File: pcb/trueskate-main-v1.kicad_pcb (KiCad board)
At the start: 2 copper layers, 160 x 120 mm, 153 parts, among them J1 Teensy 4.1 FEMALE 1x24, J11 Mini v1.0 FEMALE sockets, J12 Mini v1.0 FEMALE sockets, J13 Mini v1.0 FEMALE sockets, J14 Mini v1.0 FEMALE sockets, J15 Mini v1.0 FEMALE sockets, J16 Mini v1.0 FEMALE sockets, J2 Teensy 4.1 FEMALE 1x24, J21 MOTOR PHASES male 1x3, J22 MOTOR PHASES male 1x3, J23 MOTOR PHASES male 1x3, J24 MOTOR PHASES male 1x3, J25 MOTOR PHASES male 1x3, J26 MOTOR PHASES male 1x3, J3 VUSB from isolated Teensy pad, J31 ENCODER JST-SH 6p, J32 ENCODER JST-SH 6p, J33 ENCODER JST-SH 6p, J34 ENCODER JST-SH 6p, J35 ENCODER JST-SH 6p, J36 ENCODER JST-SH 6p, J4 NC KILL SWITCH, J41 MINI POWER: +12V / GND, J42 MINI POWER: +12V / GND, J43 MINI POWER: +12V / GND, J44 MINI POWER: +12V / GND, J45 MINI POWER: +12V / GND, J46 MINI POWER: +12V / GND, J5 12V INPUT 5.08mm >=10A, J6 WRIST: GND / 12V / DATA, J7 FUTURE I2C / 3V3 ONLY, J8 FINGERTIP 1 GND, J9 FINGERTIP 2 GND, Q1 FQP47P06 reverse-polarity, Q2 FQP47P06 servo power switch, Q3 MMBT3904 transmit enable, Q4 MMBT3904 kill power control, U1 SN74LVC08APWR, U2 SN74LVC08APWR, U3 SN74LVC1G17DBVR, U4 AP63205WU-7 fixed 5V, U5 SN74AHCT1G125DBVR TX, U6 SN74LVC1G125DBVR RX

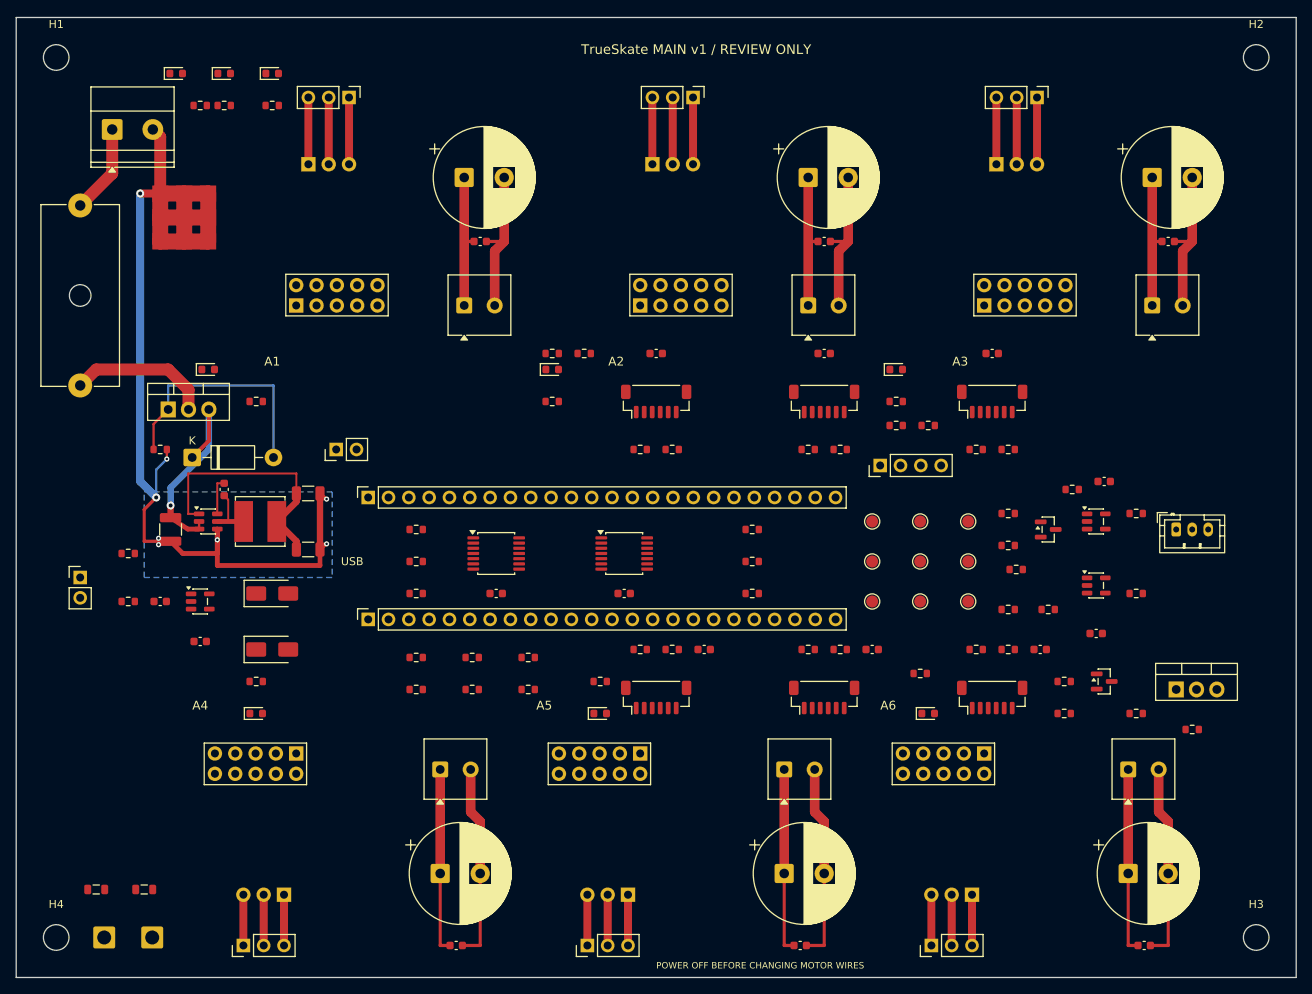
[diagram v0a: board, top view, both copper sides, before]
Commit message: feat: finish through-hole six-axis carrier review design
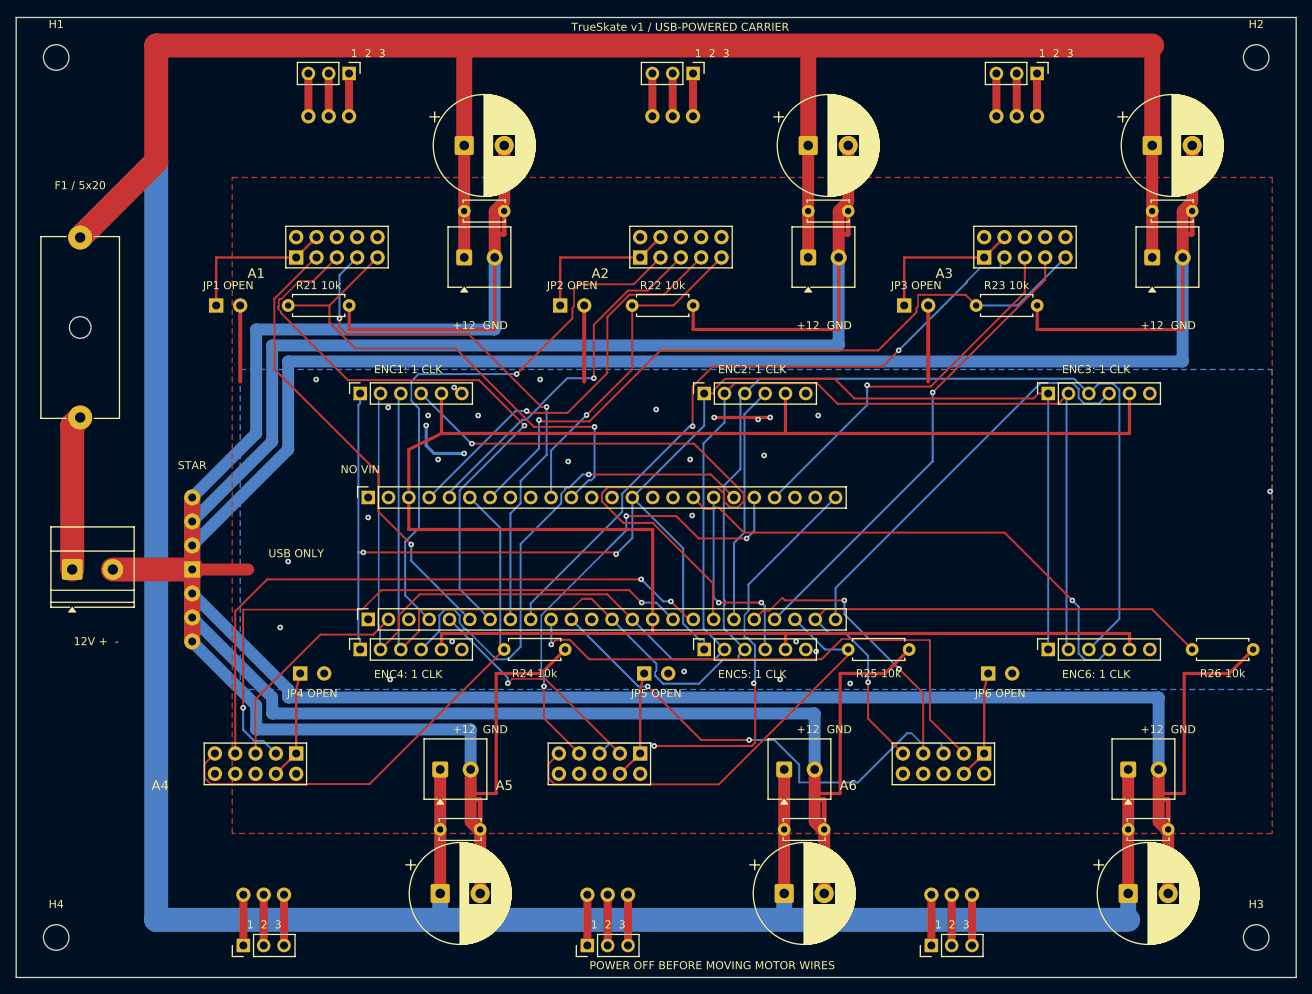
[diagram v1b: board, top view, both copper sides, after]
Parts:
- removed C1: 1nF 50V, Capacitor_SMD:C_0603_1608Metric
- removed C2, C3, C31, C32, C33, C34, C35, C36, C37, C38, C4: 100nF 50V, Capacitor_SMD:C_0603_1608Metric
- removed C5: 10uF 50V X7R, Capacitor_SMD:C_1210_3225Metric
- removed C6: 100nF bootstrap, Capacitor_SMD:C_0603_1608Metric
- removed C7, C8: 22uF 25V X5R, Capacitor_SMD:C_1206_3216Metric
- removed D1, D2: SS14 Schottky, Diode_SMD:D_SMA
- removed D11, D12, D13, D14, D15, D16, D17, D18, D19: KT-0603R red indicator, LED_SMD:LED_0603_1608Metric
- removed D3: 1N4742A 12V gate clamp, Diode_THT:D_DO-41_SOD81_P10.16mm_Horizontal
- removed FB1, FB2: BLM21PG221SN1D ferrite, Inductor_SMD:L_0805_2012Metric
- removed J3: VUSB from isolated Teensy pad, Connector_PinHeader_2.54mm:PinHeader_1x02_P2.54mm_Vertical
- removed J4: NC KILL SWITCH, Connector_PinHeader_2.54mm:PinHeader_1x02_P2.54mm_Vertical
- removed J6: WRIST: GND / 12V / DATA, Connector_JST:JST_PH_B3B-PH-K_1x03_P2.00mm_Vertical
- removed J7: FUTURE I2C / 3V3 ONLY, Connector_PinHeader_2.54mm:PinHeader_1x04_P2.54mm_Vertical
- removed J8: FINGERTIP 1 GND, Connector_Wire:SolderWire-1sqmm_1x01_D1.4mm_OD2.7mm
- removed J9: FINGERTIP 2 GND, Connector_Wire:SolderWire-1sqmm_1x01_D1.4mm_OD2.7mm
- removed L1: SRN6045TA-4R7M 4.7uH, Inductor_SMD:L_Bourns_SRN6045TA
- removed Q1: FQP47P06 reverse-polarity, Package_TO_SOT_THT:TO-220-3_Vertical
- removed Q2: FQP47P06 servo power switch, Package_TO_SOT_THT:TO-220-3_Vertical
- removed Q3: MMBT3904 transmit enable, Package_TO_SOT_SMD:SOT-23
- removed Q4: MMBT3904 kill power control, Package_TO_SOT_SMD:SOT-23
- removed R1: 1k, Resistor_SMD:R_0603_1608Metric
- removed R11, R12, R13, R14, R15, R16: 10k EN boot pulldown, Resistor_SMD:R_0603_1608Metric
- removed R2, R4, R52, R6: 10k, Resistor_SMD:R_0603_1608Metric
- removed R3, R5, R53: 100k, Resistor_SMD:R_0603_1608Metric
- removed R31, R32, R33, R34, R35, R36: 10k CS idle pullup, Resistor_SMD:R_0603_1608Metric
- removed R41, R42, R43, R44, R45, R46: 33R CS source damping, Resistor_SMD:R_0603_1608Metric
- removed R51: 100k gate off, Resistor_SMD:R_0603_1608Metric
- removed R54, R55: 4.7k, Resistor_SMD:R_0603_1608Metric
- removed R56, R57: 33R source damping, Resistor_SMD:R_0603_1608Metric
- removed R58: 10k TX boot pulldown, Resistor_SMD:R_0603_1608Metric
- removed R59: 100k bus off-state bias, Resistor_SMD:R_0603_1608Metric
- removed R60: 10k UART idle pullup, Resistor_SMD:R_0603_1608Metric
- removed R61, R62, R63, R64, R65, R66, R67, R68, R69: 4.7k LED limit, Resistor_SMD:R_0603_1608Metric
- removed R7: 100R bus series, Resistor_SMD:R_0603_1608Metric
- removed R8: 2.2k bus idle pullup / DNP, Resistor_SMD:R_0603_1608Metric
- removed R9: 10k gate sink, Resistor_SMD:R_0603_1608Metric
- removed TP1: GND, TestPoint:TestPoint_Pad_D1.5mm
- removed TP2: 12V_PROTECTED, TestPoint:TestPoint_Pad_D1.5mm
- removed TP3: BUCK_5V, TestPoint:TestPoint_Pad_D1.5mm
- removed TP4: VIN_OR, TestPoint:TestPoint_Pad_D1.5mm
- removed TP5: 3V3, TestPoint:TestPoint_Pad_D1.5mm
- removed TP6: SPI_SCK_CABLE, TestPoint:TestPoint_Pad_D1.5mm
- removed TP7: SPI_MOSI_CABLE, TestPoint:TestPoint_Pad_D1.5mm
- removed TP8: SPI_MISO, TestPoint:TestPoint_Pad_D1.5mm
- removed TP9: KILL_OK, TestPoint:TestPoint_Pad_D1.5mm
- removed U1, U2: SN74LVC08APWR, Package_SO:TSSOP-14_4.4x5mm_P0.65mm
- removed U3: SN74LVC1G17DBVR, Package_TO_SOT_SMD:SOT-23-5
- removed U4: AP63205WU-7 fixed 5V, Package_TO_SOT_SMD:TSOT-23-6
- removed U5: SN74AHCT1G125DBVR TX, Package_TO_SOT_SMD:SOT-23-5
- removed U6: SN74LVC1G125DBVR RX, Package_TO_SOT_SMD:SOT-23-5
- added JP1: CONTROL GND / OPEN, TrueSkate:GroundBridge_THT, F.Cu at (25.0, 36.0)
- added JP2: CONTROL GND / OPEN, TrueSkate:GroundBridge_THT, F.Cu at (68.0, 36.0)
- added JP3: CONTROL GND / OPEN, TrueSkate:GroundBridge_THT, F.Cu at (111.0, 36.0)
- added JP4: CONTROL GND / OPEN, TrueSkate:GroundBridge_THT, F.Cu at (35.5, 82.0)
- added JP5: CONTROL GND / OPEN, TrueSkate:GroundBridge_THT, F.Cu at (78.5, 82.0)
- added JP6: CONTROL GND / OPEN, TrueSkate:GroundBridge_THT, F.Cu at (121.5, 82.0)
- C11, C12, C13, C14, C15, C16: value EEUFR1V102B 1000uF 35V -> 1000uF 35V EEUFR1V102B
- C21, C22, C23, C24, C25, C26: value 100nF 50V -> 100nF 50V ceramic; footprint Capacitor_SMD:C_0603_1608Metric -> Capacitor_THT:C_Disc_D5.0mm_W2.5mm_P5.00mm
- F1: value 5A time-delay fuse / VERIFY -> 5x20 fuse holder / fuse TBD
- J31, J32, J33, J34, J35, J36: value ENCODER JST-SH 6p -> ENCODER breakout FEMALE 1x6; footprint Connector_JST:JST_SH_BM06B-SRSS-TB_1x06-1MP_P1.00mm_Vertical -> Connector_PinSocket_2.54mm:PinSocket_1x06_P2.54mm_Vertical
- J41, J42, J43, J44, J45, J46: value MINI POWER: +12V / GND -> MINI POWER +12V / GND
- J5: value 12V INPUT 5.08mm >=10A -> 12V INPUT + / -
- NT1: value GROUND STAR / dedicated copper -> GROUND STAR / PCB COPPER
- R21, R22, R23, R24, R25, R26: value 10k EN output pulldown -> 10k EN pull-down; footprint Resistor_SMD:R_0603_1608Metric -> Resistor_THT:R_Axial_DIN0207_L6.3mm_D2.5mm_P7.62mm_Horizontal
- moved R26 83.2 mm to (147.0, 79.0)
- moved R23 71.2 mm to (120.0, 36.0)
- moved J5 55.2 mm to (7.00, 69.0)
- moved R22 48.3 mm to (77.0, 36.0)
- moved R25 47.3 mm to (104.0, 79.0)
- moved NT1 47.2 mm to (22.0, 69.0)
- moved R21 46.8 mm to (34.0, 36.0)
- moved J34 37.5 mm to (43.0, 79.0), turned to 90 degrees
- moved J31 37.0 mm to (43.0, 47.0), turned to 90 degrees
- moved F1 26.5 mm to (8.00, 50.0), turned to 90 degrees
- moved J35 16.2 mm to (86.0, 79.0), turned to 90 degrees
- moved J32 15.0 mm to (86.0, 47.0), turned to 90 degrees
- moved C24 14.6 mm to (53.0, 101.5)
- moved C25 14.6 mm to (96.0, 101.5)
- moved C26 14.6 mm to (139.0, 101.5)
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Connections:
- C11 pad 1: 12V_PROTECTED -> 12V_FUSED
- C12 pad 1: 12V_PROTECTED -> 12V_FUSED
- C13 pad 1: 12V_PROTECTED -> 12V_FUSED
- C14 pad 1: 12V_PROTECTED -> 12V_FUSED
- C15 pad 1: 12V_PROTECTED -> 12V_FUSED
- C16 pad 1: 12V_PROTECTED -> 12V_FUSED
- C21 pad 1: 12V_PROTECTED -> 12V_FUSED
- C22 pad 1: 12V_PROTECTED -> 12V_FUSED
- C23 pad 1: 12V_PROTECTED -> 12V_FUSED
- C24 pad 1: 12V_PROTECTED -> 12V_FUSED
- C25 pad 1: 12V_PROTECTED -> 12V_FUSED
- C26 pad 1: 12V_PROTECTED -> 12V_FUSED
- J1 pad 12: KILL_OK -> unconnected-(J1-10-Pad12)
- J1 pad 22: A5_EN_REQ -> A5_EN
- J1 pad 23: A6_EN_REQ -> A6_EN
- J1 pad 3: (no net) -> unconnected-(J1-1-Pad3)
- J11 pad 1: (no net) -> CGND1
- J11 pad 10: (no net) -> unconnected-(J11-Pad10)
- J11 pad 2: (no net) -> unconnected-(J11-Pad2)
- J11 pad 4: (no net) -> CGND1
- J11 pad 6: (no net) -> unconnected-(J11-Pad6)
- J11 pad 8: (no net) -> unconnected-(J11-Pad8)
- J12 pad 1: (no net) -> CGND2
- J12 pad 10: (no net) -> unconnected-(J12-Pad10)
- J12 pad 2: (no net) -> unconnected-(J12-Pad2)
- J12 pad 4: (no net) -> CGND2
- J12 pad 6: (no net) -> unconnected-(J12-Pad6)
- J12 pad 8: (no net) -> unconnected-(J12-Pad8)
- J13 pad 1: (no net) -> CGND3
- J13 pad 10: (no net) -> unconnected-(J13-Pad10)
- J13 pad 2: (no net) -> unconnected-(J13-Pad2)
- J13 pad 4: (no net) -> CGND3
- J13 pad 6: (no net) -> unconnected-(J13-Pad6)
- J13 pad 8: (no net) -> unconnected-(J13-Pad8)
- J14 pad 1: (no net) -> CGND4
- J14 pad 10: (no net) -> unconnected-(J14-Pad10)
- J14 pad 2: (no net) -> unconnected-(J14-Pad2)
- J14 pad 4: (no net) -> CGND4
- J14 pad 6: (no net) -> unconnected-(J14-Pad6)
- J14 pad 8: (no net) -> unconnected-(J14-Pad8)
- J15 pad 1: (no net) -> CGND5
- J15 pad 10: (no net) -> unconnected-(J15-Pad10)
- J15 pad 2: (no net) -> unconnected-(J15-Pad2)
- J15 pad 4: (no net) -> CGND5
- J15 pad 6: (no net) -> unconnected-(J15-Pad6)
- J15 pad 8: (no net) -> unconnected-(J15-Pad8)
- J16 pad 1: (no net) -> CGND6
- J16 pad 10: (no net) -> unconnected-(J16-Pad10)
- J16 pad 2: (no net) -> unconnected-(J16-Pad2)
- J16 pad 4: (no net) -> CGND6
- J16 pad 6: (no net) -> unconnected-(J16-Pad6)
- J16 pad 8: (no net) -> unconnected-(J16-Pad8)
- J2 pad 1: VIN_OR -> unconnected-(J2-VIN-Pad1)
- J2 pad 10: A2_EN_REQ -> A2_EN
- J2 pad 11: A1_EN_REQ -> A1_EN
- J2 pad 12: (no net) -> unconnected-(J2-15-Pad12)
- J2 pad 13: (no net) -> unconnected-(J2-14-Pad13)
- J2 pad 16: WRIST_TX_ENABLE -> unconnected-(J2-41-Pad16)
- J2 pad 22: WRIST_TX -> unconnected-(J2-35-Pad22)
- J2 pad 23: WRIST_RX -> unconnected-(J2-34-Pad23)
- J2 pad 6: A4_EN_REQ -> A4_EN
- J2 pad 7: A3_EN_REQ -> A3_EN
- J2 pad 8: LINK_SCL -> unconnected-(J2-19-Pad8)
- J2 pad 9: LINK_SDA -> unconnected-(J2-18-Pad9)
- J31 pad 1: SPI_SCK_CABLE -> SPI_SCK
- J31 pad 3: SPI_MOSI_CABLE -> SPI_MOSI
- J31 pad 4: A1_CS_CABLE -> A1_CS
- J32 pad 1: SPI_SCK_CABLE -> SPI_SCK
- J32 pad 3: SPI_MOSI_CABLE -> SPI_MOSI
- J32 pad 4: A2_CS_CABLE -> A2_CS
- J33 pad 1: SPI_SCK_CABLE -> SPI_SCK
- J33 pad 3: SPI_MOSI_CABLE -> SPI_MOSI
- J33 pad 4: A3_CS_CABLE -> A3_CS
- J34 pad 1: SPI_SCK_CABLE -> SPI_SCK
- J34 pad 3: SPI_MOSI_CABLE -> SPI_MOSI
- J34 pad 4: A4_CS_CABLE -> A4_CS
- J35 pad 1: SPI_SCK_CABLE -> SPI_SCK
- J35 pad 3: SPI_MOSI_CABLE -> SPI_MOSI
- J35 pad 4: A5_CS_CABLE -> A5_CS
- J36 pad 1: SPI_SCK_CABLE -> SPI_SCK
- J36 pad 3: SPI_MOSI_CABLE -> SPI_MOSI
- J36 pad 4: A6_CS_CABLE -> A6_CS
- J41 pad 1: 12V_PROTECTED -> 12V_FUSED
- J42 pad 1: 12V_PROTECTED -> 12V_FUSED
- J43 pad 1: 12V_PROTECTED -> 12V_FUSED
- J44 pad 1: 12V_PROTECTED -> 12V_FUSED
- J45 pad 1: 12V_PROTECTED -> 12V_FUSED
- J46 pad 1: 12V_PROTECTED -> 12V_FUSED
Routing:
- net 12V_FUSED: track 17.9 -> 558.0 mm
- net 3V3: track 0.00 -> 251.0 mm
- net SPI_MOSI: track 0.00 -> 204.4 mm
- net SPI_MISO: track 0.00 -> 194.7 mm
- net SPI_SCK: track 0.00 -> 189.5 mm, vias 0 -> 2
- net PGND3: track 26.7 -> 204.5 mm
- net 12V_PROTECTED: track 172.7 -> 0.00 mm, vias 1 -> 0
- net PGND6: track 24.7 -> 191.5 mm
- net PGND2: track 26.7 -> 159.6 mm
- net PGND5: track 24.7 -> 146.7 mm
- net A1_CS: track 0.00 -> 90.2 mm, vias 0 -> 1
- net A3_EN: track 0.00 -> 88.8 mm, vias 0 -> 1
- net PGND1: track 26.7 -> 114.8 mm
- net A3_PWM1: track 0.00 -> 83.9 mm, vias 0 -> 2
- net A4_PWM3: track 0.00 -> 78.8 mm, vias 0 -> 2
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- added copper zone on F.Cu, net GND
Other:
- board text added: "+12 GND"
- board text added: "1 2 3"
- board text added: "12V + -"
- board text added: "50 mm between ticks - check print scale"
- board text added: "ENC1: 1 CLK"
- board text added: "ENC2: 1 CLK"
- board text added: "ENC3: 1 CLK"
- board text added: "ENC4: 1 CLK"
- board text added: "ENC5: 1 CLK"
- board text added: "ENC6: 1 CLK"
- board text added: "F1 / 5x20"
- board text added: "JP1 OPEN"
- board text added: "JP2 OPEN"
- board text added: "JP3 OPEN"
- board text added: "JP4 OPEN"
- board text added: "JP5 OPEN"
- board text added: "JP6 OPEN"
- board text added: "NO VIN"
- board text added: "POWER OFF BEFORE MOVING MOTOR WIRES"
- board text added: "R21 10k"
- board text added: "R22 10k"
- board text added: "R23 10k"
- board text added: "R24 10k"
- board text added: "R25 10k"
- board text added: "R26 10k"
- board text added: "STAR"
- board text added: "TOP VIEW / PRINT 100% / NOT MIRRORED"
- board text added: "TrueSkate v1 / USB-POWERED CARRIER"
- board text added: "USB ONLY"
- board text removed: "160 x 120 mm carrier / PAPER FIT ONLY / NOT FOR FABRICATION"
- board text removed: "50 mm between tick centres - measure before checking pins"
- board text removed: "A1 MINI"
- board text removed: "A2 MINI"
- board text removed: "A3 MINI"
- board text removed: "A4 MINI"
- board text removed: "A5 MINI"
- board text removed: "A6 MINI"
- board text removed: "POWER OFF BEFORE CHANGING MOTOR WIRES"
- board text removed: "PRINT AT 100% / ACTUAL SIZE - DO NOT FIT TO PAGE"
- board text removed: "TOP VIEW / COMPONENT SIDE / NOT MIRRORED"
- board text removed: "Teensy: USB LEFT"
- board text removed: "TrueSkate MAIN v1 / REVIEW ONLY"
- board text removed: "USB"

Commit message: feat: use exact Mini v1.0 footprints with direct power routing
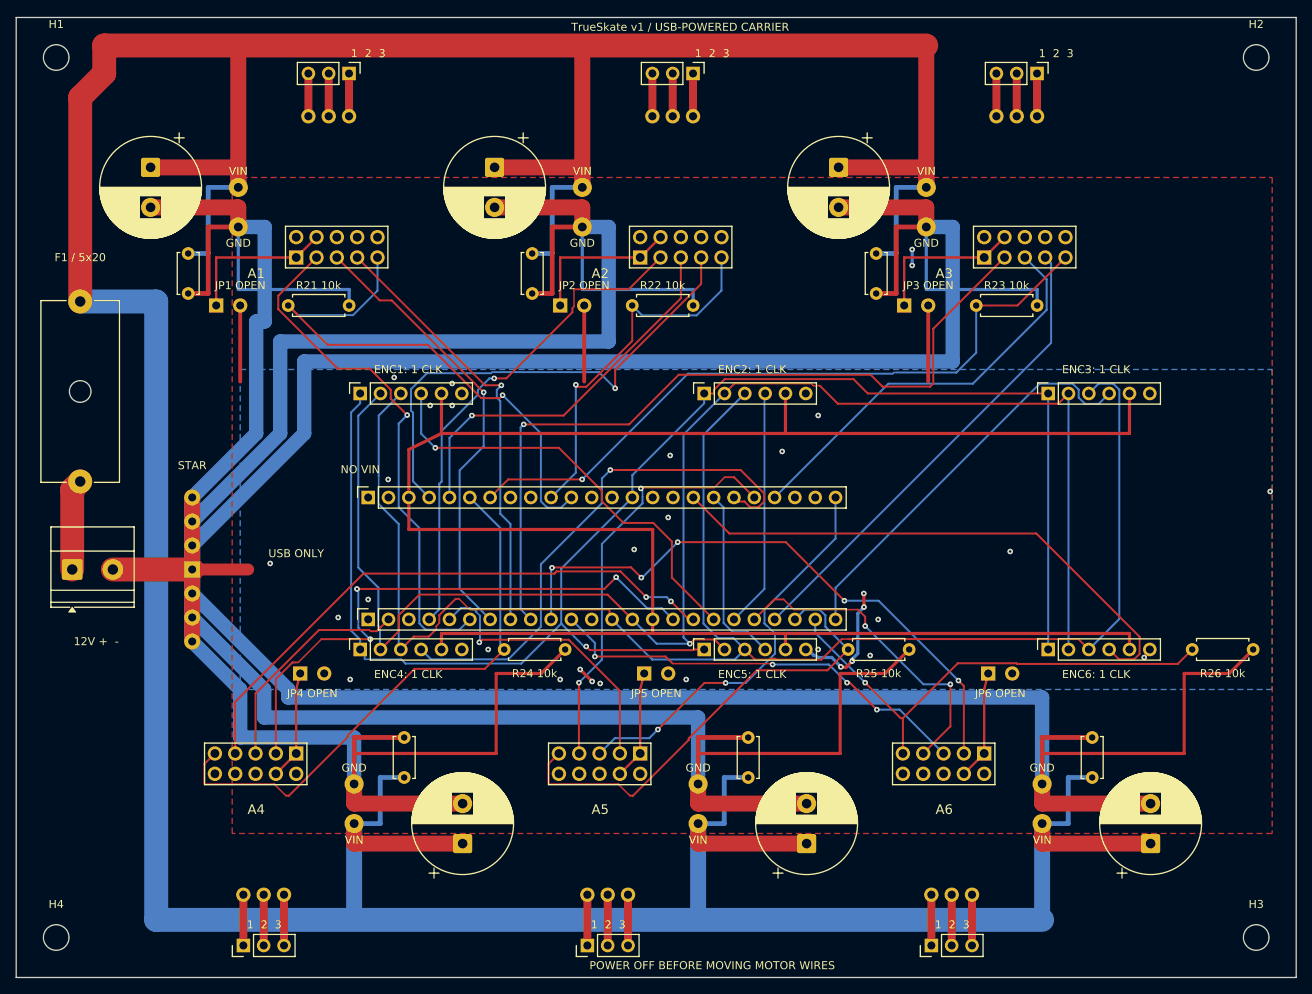
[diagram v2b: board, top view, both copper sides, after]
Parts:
- removed J41, J42, J43, J44, J45, J46: MINI POWER +12V / GND, TerminalBlock_Phoenix:TerminalBlock_Phoenix_MKDS-1-2-3.81_1x02_P3.81mm_Horizontal
- J11, J12, J13, J14, J15, J16: value Mini v1.0 FEMALE sockets -> Mini v1.0 / 15-hole socket; footprint TrueSkate:Mini_v1_Sockets -> TrueSkate:SimpleFOC_Mini_v1.0
- moved C11 39.3 mm to (16.8, 18.7), turned to -90 degrees
- moved C12 39.3 mm to (59.8, 18.7), turned to -90 degrees
- moved C13 39.3 mm to (102.8, 18.7), turned to -90 degrees
- moved C21 34.9 mm to (21.5, 29.5), turned to -90 degrees
- moved C22 34.9 mm to (64.5, 29.5), turned to -90 degrees
- moved C23 34.9 mm to (107.5, 29.5), turned to -90 degrees
- moved J14 10.2 mm to (24.8, 92.0)
- moved J11 10.2 mm to (45.2, 30.0)
- moved J12 10.2 mm to (88.2, 30.0)
- moved J13 10.2 mm to (131.2, 30.0)
- moved J15 10.2 mm to (67.8, 92.0)
- moved J16 10.2 mm to (110.8, 92.0)
- moved F1 8.00 mm to (8.00, 58.0)
- moved C24 7.91 mm to (48.5, 95.0), turned to 90 degrees
- moved C25 7.91 mm to (91.5, 95.0), turned to 90 degrees
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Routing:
- net A1_CS: track 90.2 -> 54.6 mm
- net 12V_FUSED: track 558.0 -> 591.1 mm
- net PGND3: track 204.5 -> 181.6 mm
- net PGND2: track 159.6 -> 137.4 mm
- net PGND1: track 114.8 -> 93.1 mm
- net A1_PWM2: track 76.7 -> 56.5 mm
- net A3_PWM1: track 83.9 -> 99.1 mm, vias 2 -> 1
- net A1_PWM3: track 68.1 -> 54.8 mm, vias 2 -> 1
- net A2_PWM3: track 50.7 -> 62.5 mm
- net A6_EN: track 72.2 -> 61.2 mm
- net A2_PWM1: track 71.7 -> 62.5 mm
- net 12V_IN: track 19.4 -> 11.4 mm
- net A1_PWM1: track 57.6 -> 65.4 mm
- net A6_PWM1: track 68.8 -> 76.3 mm, vias 1 -> 5
- net A5_PWM1: track 29.1 -> 36.4 mm
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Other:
- board text removed: "+12 GND"
